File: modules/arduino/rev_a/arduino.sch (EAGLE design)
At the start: 63 parts, among them J1 MODULE_GENERIC, J3 ICSP_PROG, J4 MICRO_USB_B_HIROSE_ZX62-B-5PA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, J6 ICSP, U1 ATMEGA8U2-MU, U2 ATMEGA328P-20MU, U3 ADG3304, U4 ADG3304, U5 74LVC2G00DC, U6 SN74LVC1G123DCUR, Y1 12 MHz, Y2 16MHz

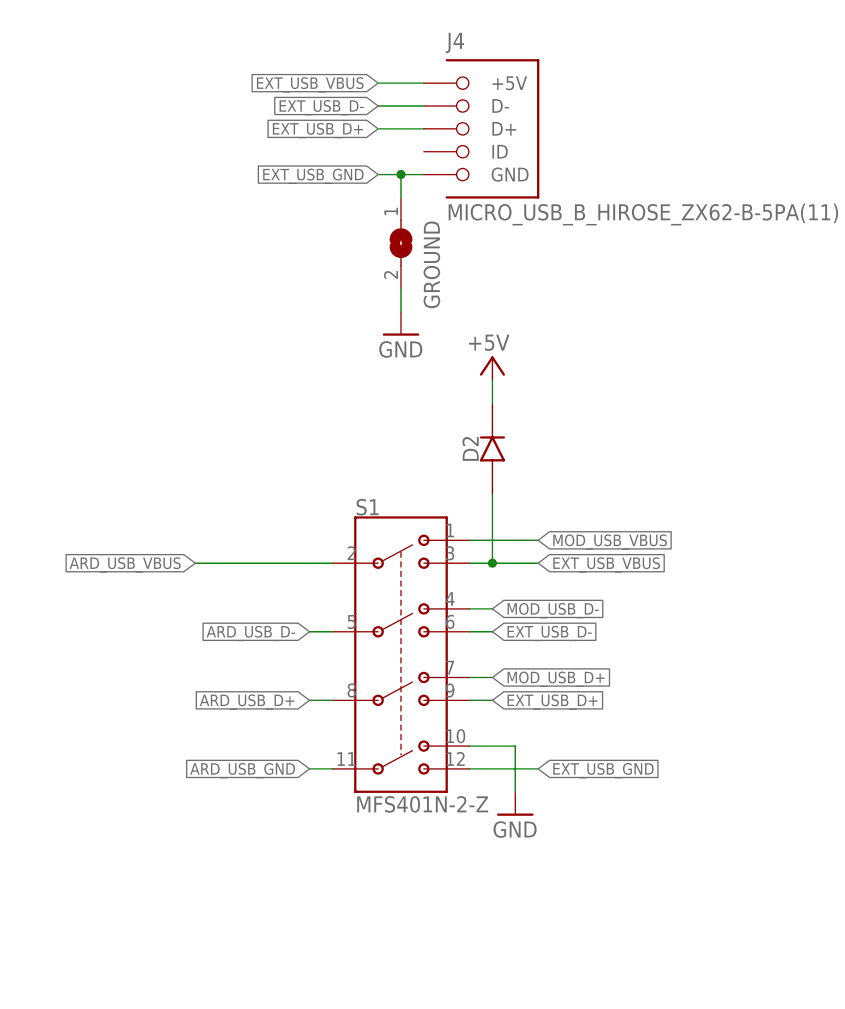
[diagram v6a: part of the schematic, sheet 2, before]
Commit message: Seinduino: Curve USB, tighten up dimension layer
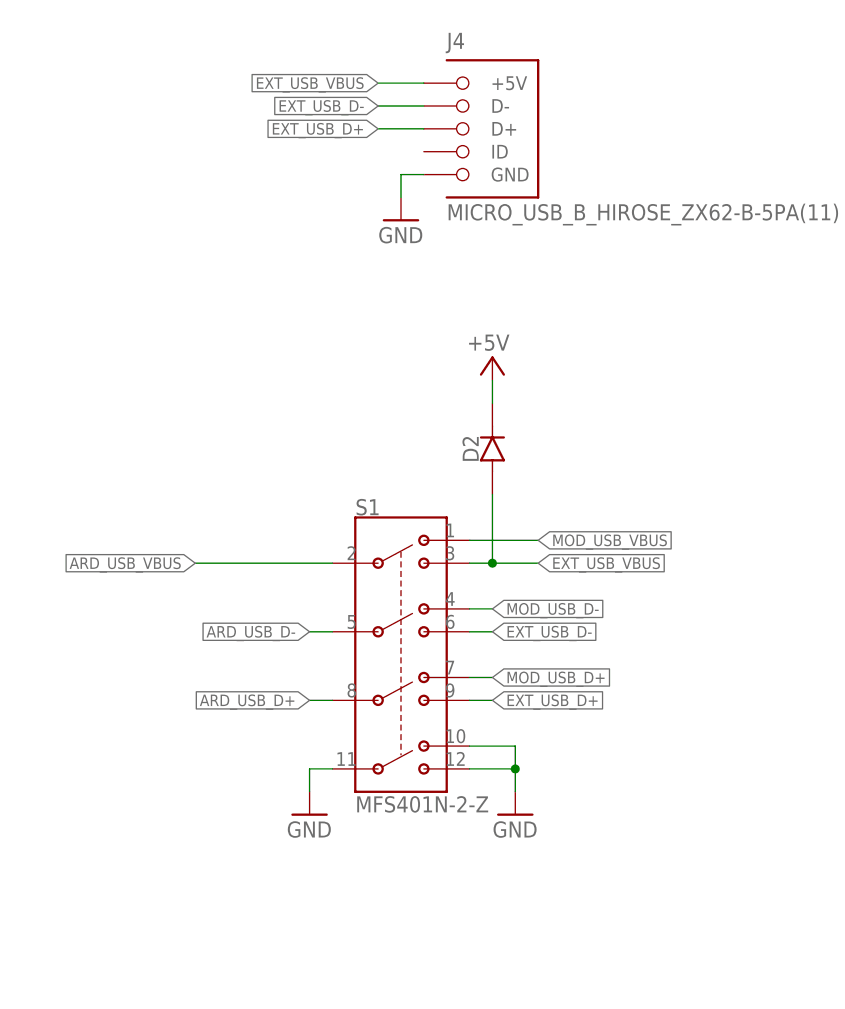
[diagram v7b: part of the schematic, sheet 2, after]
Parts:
- removed GROUND: (no value), jumper:SJ
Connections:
- removed net ARD_USB_GND: C8.2, S1.4P, U1.UGND
- removed net EXT_USB_GND: GROUND.1, J4.GND, S1.4TB
- net GND: now also C8.2, J4.GND, S1.4P, S1.4TB, U1.UGND; no longer GROUND.2
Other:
- note added: "Remove USB Connector Rename USB signals XUSB -> ARD_USB_VBUS D- -> ARD_USB_D- D+ -> ARD_USB_D+ UGND-> GND USHIELD -> (nil)"
- note removed: "Remove USB Connector Rename USB signals XUSB -> ARD_USB_VBUS D- -> ARD_USB_D- D+ -> ARD_USB_D+ UGND-> ARD_USB_GND USHIELD -> (nil)"
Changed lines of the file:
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@@
 <attribute name="DIGIKEY" value="490-1198-1-ND"/>
 </part>
-<part name="GROUND" library="jumper" deviceset="SJ" device=""/>
 <part name="RESET-PROG-EN" library="jumper" deviceset="SJ" device=""/>
 <part name="R2" library="SmartPrj" deviceset="R-EU_" device="R0603" value="1M"/>
@@
 <part name="R11" library="passives" deviceset="RESISTOR" device="0603_RES" value="1kΩ"/>
 <part name="R12" library="passives" deviceset="RESISTOR" device="0603_RES" value="1kΩ"/>
+<part name="GND21" library="supply1" deviceset="GND" device=""/>
+<part name="GND25" library="umich" deviceset="GND" device=""/>
 </parts>
 <sheets>
@@
  D-       -&gt; ARD_USB_D-
  D+      -&gt; ARD_USB_D+
- UGND-&gt; ARD_USB_GND
+ UGND-&gt; GND
 USHIELD -&gt; (nil)</text>
 <wire x1="-48.26" y1="101.6" x2="-48.26" y2="50.8" width="0.508" layer="98"/>
@@
 <instance part="R11" gate="G$1" x="238.76" y="10.16"/>
 <instance part="R12" gate="G$1" x="246.38" y="5.08"/>
+<instance part="GND21" gate="1" x="60.96" y="12.7"/>
 </instances>
 <busses>
@@
 <pinref part="GND18" gate="1" pin="GND"/>
 <wire x1="482.6" y1="-2.54" x2="482.6" y2="-5.08" width="0.1524" layer="91"/>
+</segment>
+<segment>
+<wire x1="60.96" y1="17.78" x2="71.12" y2="17.78" width="0.1524" layer="91"/>
+<wire x1="71.12" y1="17.78" x2="71.12" y2="30.48" width="0.1524" layer="91"/>
+<wire x1="71.12" y1="30.48" x2="91.44" y2="30.48" width="0.1524" layer="91"/>
+<wire x1="60.96" y1="27.94" x2="60.96" y2="17.78" width="0.1524" layer="91"/>
+<junction x="60.96" y="17.78"/>
+<pinref part="U1" gate="G$1" pin="UGND"/>
+<pinref part="C8" gate="G$1" pin="2"/>
+<pinref part="GND21" gate="1" pin="GND"/>
+<wire x1="60.96" y1="15.24" x2="60.96" y2="17.78" width="0.1524" layer="91"/>
 </segment>
 </net>
@@
 <wire x1="469.9" y1="76.2" x2="464.82" y2="76.2" width="0.1524" layer="91"/>
 <label x="469.9" y="76.2" size="1.27" layer="95" xref="yes"/>
-</segment>
-</net>
-<net name="ARD_USB_GND" class="2">
-<segment>
-<wire x1="58.42" y1="17.78" x2="60.96" y2="17.78" width="0.1524" layer="91"/>
-<wire x1="60.96" y1="17.78" x2="71.12" y2="17.78" width="0.1524" layer="91"/>
-<wire x1="71.12" y1="17.78" x2="71.12" y2="30.48" width="0.1524" layer="91"/>
-<wire x1="71.12" y1="30.48" x2="91.44" y2="30.48" width="0.1524" layer="91"/>
-<wire x1="60.96" y1="27.94" x2="60.96" y2="17.78" width="0.1524" layer="91"/>
-<junction x="60.96" y="17.78"/>
-<pinref part="U1" gate="G$1" pin="UGND"/>
-<pinref part="C8" gate="G$1" pin="2"/>
-<label x="58.42" y="17.78" size="1.27" layer="95" rot="R180" xref="yes"/>
-</segment>
-<segment>
-<wire x1="20.32" y1="55.88" x2="35.56" y2="55.88" width="0.1524" layer="91"/>
-<wire x1="20.32" y1="60.96" x2="20.32" y2="55.88" width="0.1524" layer="91"/>
-<wire x1="-5.08" y1="60.96" x2="20.32" y2="60.96" width="0.1524" layer="91"/>
-<label x="0" y="60.96" size="1.778" layer="95"/>
-<label x="-5.08" y="60.96" size="1.27" layer="95" rot="R180" xref="yes"/>
-<label x="35.56" y="55.88" size="1.27" layer="95" xref="yes"/>
 </segment>
 </net>
@@
 <attribute name="VALUE" x="24.765" y="55.88" size="1.778" layer="96" rot="R180"/>
 </instance>
-<instance part="GROUND" gate="1" x="185.42" y="106.68" rot="R270"/>
-<instance part="GND6" gate="1" x="185.42" y="96.52"/>
+<instance part="GND6" gate="1" x="185.42" y="109.22"/>
 <instance part="D1" gate="G$1" x="43.18" y="96.52">
 <attribute name="DIGIKEY" x="43.18" y="96.52" size="1.27" layer="96" font="vector" display="off"/>
@@
 </instance>
 <instance part="LOGO1" gate="G$1" x="2.54" y="172.72"/>
+<instance part="GND25" gate="1" x="175.26" y="43.18"/>
 </instances>
 <busses>
@@
 <pinref part="GND28" gate="1" pin="GND"/>
 <wire x1="193.04" y1="50.8" x2="198.12" y2="50.8" width="0.1524" layer="91"/>
-<wire x1="198.12" y1="50.8" x2="198.12" y2="45.72" width="0.1524" layer="91"/>
-</segment>
-<segment>
-<pinref part="GROUND" gate="1" pin="2"/>
+<wire x1="198.12" y1="50.8" x2="198.12" y2="48.26" width="0.1524" layer="91"/>
+<pinref part="S1" gate="G$1" pin="4TB"/>
+<wire x1="198.12" y1="48.26" x2="198.12" y2="45.72" width="0.1524" layer="91"/>
+<wire x1="193.04" y1="48.26" x2="198.12" y2="48.26" width="0.1524" layer="91"/>
+<junction x="198.12" y="48.26"/>
+</segment>
+<segment>
+<pinref part="S1" gate="G$1" pin="4P"/>
+<pinref part="GND25" gate="1" pin="GND"/>
+<wire x1="177.8" y1="48.26" x2="175.26" y2="48.26" width="0.1524" layer="91"/>
+<wire x1="175.26" y1="48.26" x2="175.26" y2="45.72" width="0.1524" layer="91"/>
+</segment>
+<segment>
+<pinref part="J4" gate="G$1" pin="GND"/>
 <pinref part="GND6" gate="1" pin="GND"/>
-<wire x1="185.42" y1="99.06" x2="185.42" y2="101.6" width="0.1524" layer="91"/>
+<wire x1="187.96" y1="114.3" x2="185.42" y2="114.3" width="0.1524" layer="91"/>
+<wire x1="185.42" y1="114.3" x2="185.42" y2="111.76" width="0.1524" layer="91"/>
 </segment>
 </net>
@@
 </segment>
 </net>
-<net name="ARD_USB_GND" class="2">
-<segment>
-<pinref part="S1" gate="G$1" pin="4P"/>
-<wire x1="175.26" y1="48.26" x2="177.8" y2="48.26" width="0.1524" layer="91"/>
-<label x="175.26" y="48.26" size="1.27" layer="95" rot="R180" xref="yes"/>
-</segment>
-</net>
-<net name="EXT_USB_GND" class="0">
-<segment>
-<pinref part="J4" gate="G$1" pin="GND"/>
-<wire x1="182.88" y1="114.3" x2="185.42" y2="114.3" width="0.1524" layer="91"/>
-<label x="182.88" y="114.3" size="1.27" layer="95" rot="R180" xref="yes"/>
-<pinref part="GROUND" gate="1" pin="1"/>
-<wire x1="185.42" y1="114.3" x2="187.96" y2="114.3" width="0.1524" layer="91"/>
-<wire x1="185.42" y1="111.76" x2="185.42" y2="114.3" width="0.1524" layer="91"/>
-<junction x="185.42" y="114.3"/>
-</segment>
-<segment>
-<pinref part="S1" gate="G$1" pin="4TB"/>
-<wire x1="200.66" y1="48.26" x2="193.04" y2="48.26" width="0.1524" layer="91"/>
-<label x="200.66" y="48.26" size="1.27" layer="95" xref="yes"/>
-</segment>
-</net>

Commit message: seinduino: renumber / normalize components
 - Change 1MΩ resistors to all use same package
 - Renumber caps
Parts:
- removed JP1: (no value), pinhead:PINHD-1X2
- added J-ARD-I2C: (no value), pinhead:PINHD-1X2
- C1, C2: value 100nF -> 22pF; device passives:CAPACITOR0603_CAP -> SmartPrj:C-EU0603-RND
- C10: value 10uF -> 100nF; DIGIKEY 445-6853-1-ND -> (none)
- C11, C9: value 22p -> 100nF; device SmartPrj:C-EU0603-RND -> passives:CAPACITOR0603_CAP
- C12: value 22uF -> 100nF; DIGIKEY 445-9077-1-ND -> (none)
- C14: value 100nF -> 1uF; device passives:CAPACITOR0603_CAP -> SmartPrj:C-EU0603-RND
- C15: value 100nF -> 10uF; DIGIKEY (none) -> 445-6853-1-ND
- C16: value 100nF -> 22uF; DIGIKEY (none) -> 445-9077-1-ND
- C8: value 1uF -> 100nF; device SmartPrj:C-EU0603-RND -> passives:CAPACITOR0603_CAP
- R1, R2: value 1M -> 1MΩ; device SmartPrj:R-EU_R0603 -> passives:RESISTOR0603_RES
- renumbered AD to J-ARD-AD, IOH to J-ARD-IOH, IOL to J-ARD-IOL
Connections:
- net +3V3: now also C16.1; no longer C12.1
- net +5V: now also C15.1, C7.1, C9.1; no longer C1.1, C10.1, C3.1
- net AD4: now also J-ARD-I2C.2; no longer JP1.2
- net AD5: now also J-ARD-I2C.1; no longer JP1.1
- net AREF: now also C6.2; no longer C4.2
- net GND: now also C10.1, C11.1, C14.2, C15.2, C2.2, C4.2, C5.2, C6.1, C8.1; no longer C10.2, C11.2, C12.2, C14.1, C15.1, C2.1, C4.1, C6.2, C8.2
- net N$7: now also C12.2; no longer C5.2
- net VCC: now also C10.2, C11.2, C12.1, C3.1, C4.1, C8.2; no longer C14.2, C15.2, C16.1, C2.2, C6.1, C7.1
- net VUCAP: now also C14.1; no longer C8.1
- net XT1: now also C1.1; no longer C9.1
- net XT2: now also C2.1; no longer C11.1
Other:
- note added: "Leave this named "L" because people know and expect "the L LED" in Arduino"
- moved on the sheet: C13, C3, C4, C5, C6, C7
